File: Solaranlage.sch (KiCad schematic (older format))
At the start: 79 parts, among them J1 Screw_Terminal_01x02, J10 Conn_01x01_Male, J2 Screw_Terminal_01x02, J3 AVR-JTAG-10, J4 USB_B, J5 USB_B, J6 Screw_Terminal_01x02, J7 Conn_01x02_Male, J8 Conn_01x01_Male, J9 Conn_01x02_Male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

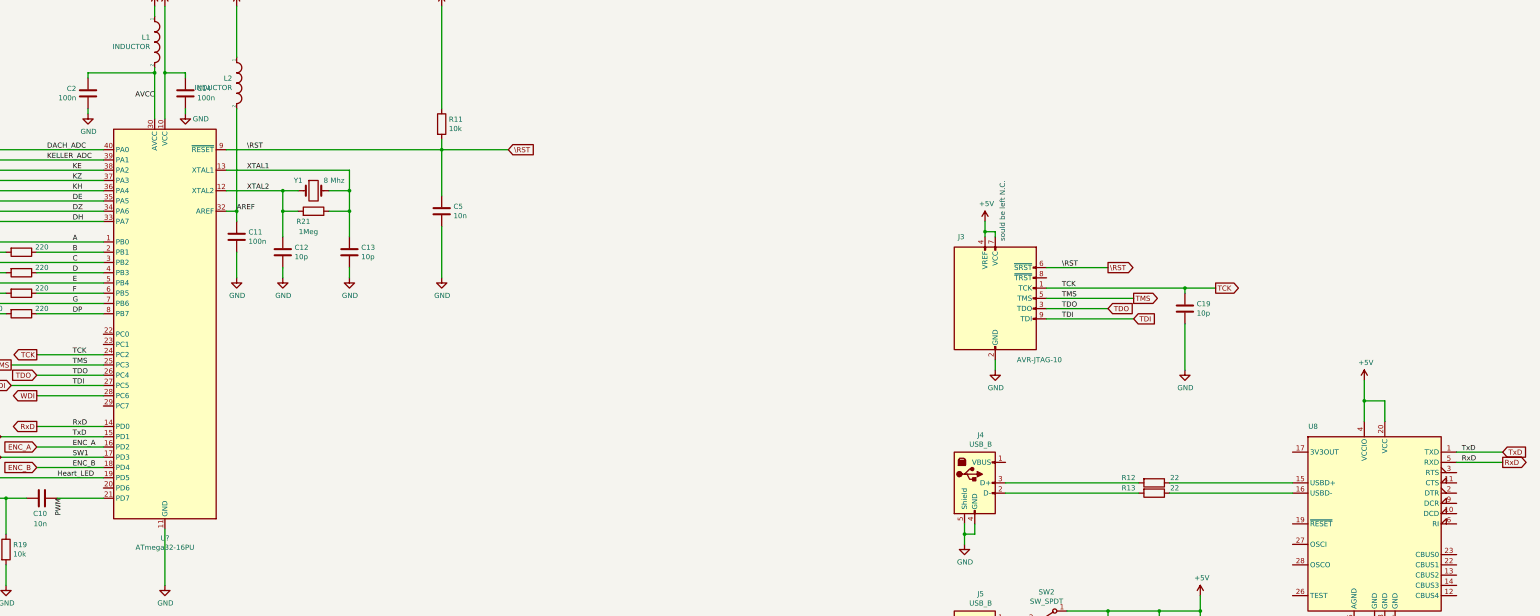
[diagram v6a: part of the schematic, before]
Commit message: added simualtion for analog amp; applied changes in footprints
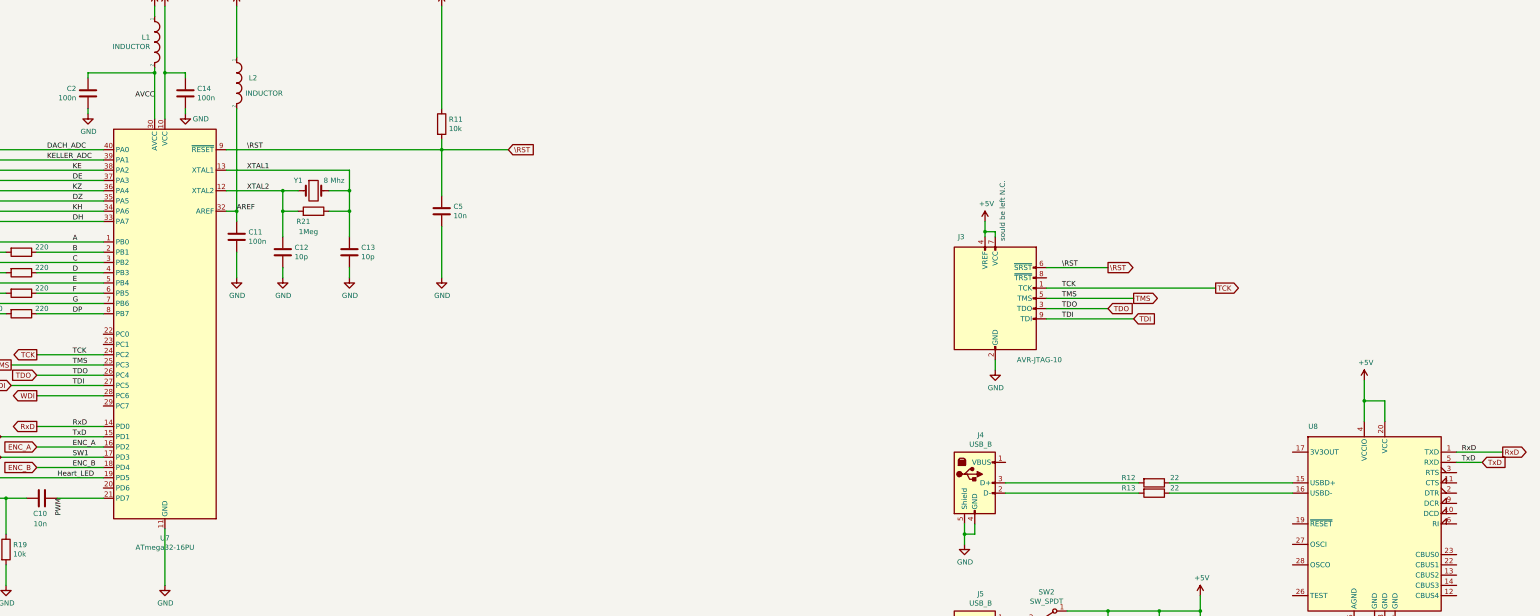
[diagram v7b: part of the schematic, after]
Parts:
- removed C19: 10p, Capacitor_THT:C_Disc_D4.7mm_W2.5mm_P5.00mm, symbol Device:C
- C1, C15: footprint Capacitor_THT:C_Rect_L9.0mm_W2.5mm_P7.50mm_MKT -> Capacitor_THT:C_Disc_D4.7mm_W2.5mm_P5.00mm
- gave numbers to parts that had none: 1
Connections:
- net DE: now also U5.3 (CC), U5.8 (CC), U7.37 (PA3); no longer U3.3 (CC), U3.8 (CC), U7.35 (PA5)
- net DZ: now also U3.3 (CC), U3.8 (CC), U7.35 (PA5); no longer U2.3 (CC), U2.8 (CC), U7.34 (PA6)
- net KH: now also U2.3 (CC), U2.8 (CC), U7.34 (PA6); no longer U4.3 (CC), U4.8 (CC), U7.36 (PA4)
- net KZ: now also U4.3 (CC), U4.8 (CC), U7.36 (PA4); no longer U5.3 (CC), U5.8 (CC), U7.37 (PA3)
- net RxD: now also U8.1 (TXD); no longer U8.5 (RXD)
- net TxD: now also U8.5 (RXD); no longer U8.1 (TXD)
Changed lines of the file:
@@
 	1    0    0    -1
 $EndComp
+Text Label 25200 6400 0    50   ~ 0
+RxD
 Text Label 25200 6500 0    50   ~ 0
-RxD
-Text Label 25200 6400 0    50   ~ 0
 TxD
 Wire Wire Line
@@
 Wire Wire Line
 	21150 5000 21750 5000
-Wire Wire Line
-	21150 4800 22500 4800
 Text Notes 20750 4350 1    50   ~ 0
 sould be left N.C.\n
@@
 	24550 8100 24550 8250
 Wire Wire Line
-	25150 6500 25600 6500
-Wire Wire Line
-	25600 6400 25150 6400
+	25150 6400 25600 6400
+Wire Wire Line
+	25400 6500 25150 6500
 $Comp
 L Interface_USB:FT232RL U8
@@
 Text Label 11650 3650 0    50   ~ 0
 KE
+Text Label 11650 3850 0    50   ~ 0
+KZ
+Text Label 11650 4050 0    50   ~ 0
+KH
 Text Label 11650 3750 0    50   ~ 0
-KZ
-Text Label 11650 3850 0    50   ~ 0
-KH
+DE
 Text Label 11650 3950 0    50   ~ 0
-DE
-Text Label 11650 4050 0    50   ~ 0
 DZ
 Text Label 11650 4150 0    50   ~ 0
@@
 Wire Wire Line
 	15250 3450 15900 3450
-Text GLabel 25600 6400 2    50   Input ~ 0
+Text GLabel 25400 6500 2    50   Input ~ 0
 TxD
-Text GLabel 25600 6500 2    50   Output ~ 0
+Text GLabel 25600 6400 2    50   Output ~ 0
 RxD
 Text GLabel 10950 6250 0    50   Input ~ 0
@@
 F 0 "C15" V 11400 11050 50  0000 L CNN
 F 1 "10n" V 11300 11050 50  0000 L CNN
-F 2 "Capacitor_THT:C_Rect_L9.0mm_W2.5mm_P7.50mm_MKT" H 11188 10950 50  0001 C CNN
+F 2 "Capacitor_THT:C_Disc_D4.7mm_W2.5mm_P5.00mm" H 11188 10950 50  0001 C CNN
 F 3 "~" H 11150 11100 50  0001 C CNN
 F 4 "" V 10950 11150 50  0001 C CNN "Ordering Code"
@@
 F 0 "C1" H 14615 11296 50  0000 L CNN
 F 1 "10n" H 14615 11205 50  0000 L CNN
-F 2 "Capacitor_THT:C_Rect_L9.0mm_W2.5mm_P7.50mm_MKT" H 14538 11100 50  0001 C CNN
+F 2 "Capacitor_THT:C_Disc_D4.7mm_W2.5mm_P5.00mm" H 14538 11100 50  0001 C CNN
 F 3 "~" H 14500 11250 50  0001 C CNN
 F 4 "" V 14300 11300 50  0001 C CNN "Ordering Code"
@@
 U 1 1 5FD19EB6
 P 13250 2800
-F 0 "L2" V 13204 2756 50  0000 R CNN
-F 1 "INDUCTOR" V 13295 2756 50  0000 R CNN
+F 0 "L2" V 13200 3000 50  0000 R CNN
+F 1 "INDUCTOR" V 13350 3250 50  0000 R CNN
 F 2 "Inductor_THT:L_Radial_D10.0mm_P5.00mm_Fastron_07P" H 13250 2800 50  0001 C CNN
 F 3 "~" H 13250 2800 50  0001 C CNN
@@
 	-1   0    0    -1
 $EndComp
-$Comp
-L Device:C C19
-U 1 1 5FB12E26
-P 22500 5000
-F 0 "C19" H 22615 5046 50  0000 L CNN
-F 1 "10p" H 22615 4955 50  0000 L CNN
-F 2 "Capacitor_THT:C_Disc_D4.7mm_W2.5mm_P5.00mm" H 22538 4850 50  0001 C CNN
-F 3 "~" H 22500 5000 50  0001 C CNN
-	1    22500 5000
-	1    0    0    -1
-$EndComp
-$Comp
-L power:GND #PWR?
-U 1 1 5FB64444
-P 22500 5600
-AR Path="/5F670D5B/5FB64444" Ref="#PWR?"  Part="1"
-AR Path="/5F671D57/5FB64444" Ref="#PWR?"  Part="1"
-AR Path="/5FB64444" Ref="#PWR02"  Part="1"
-F 0 "#PWR02" H 22500 5350 50  0001 C CNN
-F 1 "GND" H 22505 5427 50  0000 C CNN
-F 2 "" H 22500 5600 50  0001 C CNN
-F 3 "" H 22500 5600 50  0001 C CNN
-	1    22500 5600
-	1    0    0    -1
-$EndComp
-Wire Wire Line
-	22500 4800 22500 4850
-Wire Wire Line
-	22500 5150 22500 5600
-Connection ~ 22500 4800
-Wire Wire Line
-	22500 4800 22800 4800
 Wire Wire Line
 	15100 10950 14950 10950
@@
 $EndComp
 $Comp
-L MCU_Microchip_ATmega:ATmega32-16PU U?
+L MCU_Microchip_ATmega:ATmega32-16PU U7
 U 1 1 5FC9465F
 P 12550 5150
-F 0 "U?" H 12550 3061 50  0000 C CNN
+F 0 "U7" H 12550 3061 50  0000 C CNN
 F 1 "ATmega32-16PU" H 12550 2970 50  0000 C CNN
 F 2 "Package_DIP:DIP-40_W15.24mm" H 12550 5150 50  0001 C CIN
@@
 	-1   0    0    -1
 $EndComp
+Wire Wire Line
+	21150 4800 22800 4800
 $EndSCHEMATC

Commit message: added amps for measureing
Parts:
- removed J10, J8: Conn_01x01_Male, Connector_PinHeader_2.54mm:PinHeader_1x01_P2.54mm_Vertical, symbol Connector:Conn_01x01_Male
- removed J7, J9: Conn_01x02_Male, Connector_PinHeader_2.54mm:PinHeader_1x02_P2.54mm_Vertical, symbol Connector:Conn_01x02_Male
- removed JP1, JP2: Jumper, Jumper:SolderJumper-2_P1.3mm_Open_Pad1.0x1.5mm, symbol Device:Jumper
- removed R21: 1Meg, Resistor_THT:R_Axial_DIN0204_L3.6mm_D1.6mm_P7.62mm_Horizontal, symbol Device:R
- added C17, C19, C20: 10n, Capacitor_THT:C_Disc_D4.7mm_W2.5mm_P5.00mm, symbol Device:C
- added RV1, RV2: R_POT_TRIM, Potentiometer_THT:Potentiometer_Bourns_3299W_Vertical, symbol Device:R_POT_TRIM
- added U9: TS912, Package_DIP:DIP-8_W7.62mm_LongPads, symbol Amplifier_Operational:TS912
- J4, J5: symbol Connector:USB_B -> Solaranlage-rescue:USB_B-Connector
- SW1: symbol Device:Rotary_Encoder_Switch_Panasonic_EVE-QDBRL416B -> Solaranlage-rescue:Rotary_Encoder_Switch_Panasonic_EVE-QDBRL416B-Device
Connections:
- net +5V: now also C20.1, U9.8 (V+)
- net DACH_ADC: now also C17.1, RV1.1, U9.1
- net GND: now also C17.2, C19.2, C20.2, RV1.3, RV2.3, U9.4 (V-)
- net KELLER_ADC: now also C19.1, RV2.1, U9.7
- net at C4.1, J2.2 (Pin_2), R2.2: now also U9.5 (+)
- net at C3.1, J1.2 (Pin_2), R1.2: now also U9.3 (+)
- new net: RV1.2, U9.2 (-)
- new net: RV2.2, U9.6 (-)
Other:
- note added: "1.449 k"
- note added: "8.550 k"
- note added: "k = 6.9"
- note removed: "t(R) ^= 2,5*R_th – 251,75"
- moved on the sheet: C1, C10, C11, C12, C13, C14, C15, C16, C18, C2, C3, C4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
